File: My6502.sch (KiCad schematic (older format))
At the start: 38 parts, among them J1 ~NMI, J2 CLK Jumper, J3 Power 5V, J4 Expansion Bus, J5 Port A, J6 Port B, SW1 RESET, U1 ROM 28C256, U2 WD65C02, U3 RAM 62256, U4 74HCT00, U5 74HCT02, U6 DS1813-10, U7 74LS21, U8 WD65C22, X1 OSC

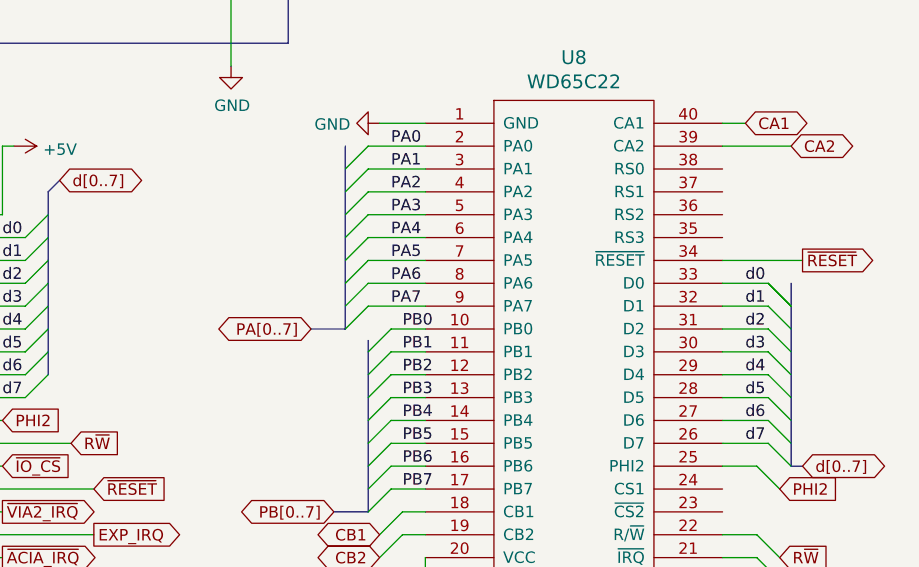
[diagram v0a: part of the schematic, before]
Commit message: Components Placed - missing wiring the VIA
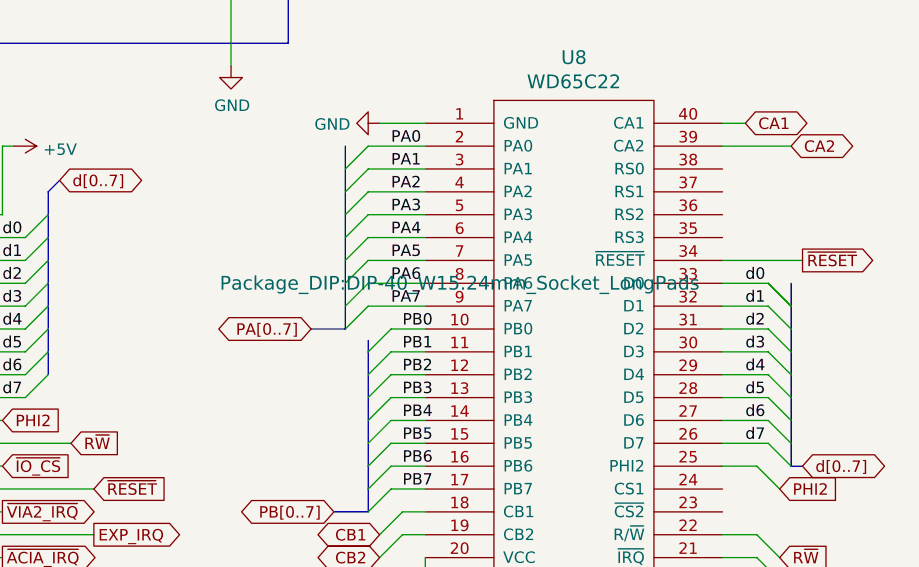
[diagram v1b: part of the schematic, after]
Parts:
- H1, H2, H3, H4: footprint (none) -> MountingHole:MountingHole_3.2mm_M3_DIN965_Pad_TopBottom
- J1: footprint (none) -> Connector_PinHeader_2.54mm:PinHeader_1x01_P2.54mm_Vertical
- TP1, TP2: footprint (none) -> TestPoint:TestPoint_THTPad_2.0x2.0mm_Drill1.0mm
- U8: footprint (none) -> Package_DIP:DIP-40_W15.24mm_Socket_LongPads
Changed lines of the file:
@@
 F 0 "TP2" V 6950 4050 50  0000 C CNN
 F 1 "~RESET" V 6850 4050 50  0000 C CNN
-F 2 "" H 7000 3800 50  0001 C CNN
+F 2 "TestPoint:TestPoint_THTPad_2.0x2.0mm_Drill1.0mm" H 7000 3800 50  0001 C CNN
 F 3 "~" H 7000 3800 50  0001 C CNN
 	1    6800 3800
@@
 F 0 "TP1" H 3602 2001 50  0000 L CNN
 F 1 "CLK" H 3602 1910 50  0000 L CNN
-F 2 "" H 3650 1900 50  0001 C CNN
+F 2 "TestPoint:TestPoint_THTPad_2.0x2.0mm_Drill1.0mm" H 3650 1900 50  0001 C CNN
 F 3 "~" H 3650 1900 50  0001 C CNN
 	1    3450 1900
@@
 F 0 "H2" V 9404 4000 50  0000 L CNN
 F 1 "MNT" V 9495 4000 50  0000 L CNN
-F 2 "" H 9450 3850 50  0001 C CNN
+F 2 "MountingHole:MountingHole_3.2mm_M3_DIN965_Pad_TopBottom" H 9450 3850 50  0001 C CNN
 F 3 "~" H 9450 3850 50  0001 C CNN
 	1    9450 3850
@@
 F 0 "H4" V 9404 4200 50  0000 L CNN
 F 1 "MNT" V 9495 4200 50  0000 L CNN
-F 2 "" H 9450 4050 50  0001 C CNN
+F 2 "MountingHole:MountingHole_3.2mm_M3_DIN965_Pad_TopBottom" H 9450 4050 50  0001 C CNN
 F 3 "~" H 9450 4050 50  0001 C CNN
 	1    9450 4050
@@
 F 0 "H1" V 9200 4100 50  0000 C CNN
 F 1 "MNT" V 9100 4100 50  0000 C CNN
-F 2 "" H 9150 3850 50  0001 C CNN
+F 2 "MountingHole:MountingHole_3.2mm_M3_DIN965_Pad_TopBottom" H 9150 3850 50  0001 C CNN
 F 3 "~" H 9150 3850 50  0001 C CNN
 	1    9150 3850
@@
 F 0 "H3" V 9200 4300 50  0000 C CNN
 F 1 "MNT" V 9100 4300 50  0000 C CNN
-F 2 "" H 9150 4050 50  0001 C CNN
+F 2 "MountingHole:MountingHole_3.2mm_M3_DIN965_Pad_TopBottom" H 9150 4050 50  0001 C CNN
 F 3 "~" H 9150 4050 50  0001 C CNN
 	1    9150 4050
@@
 F 0 "U8" H 4350 6237 60  0000 C CNN
 F 1 "WD65C22" H 4350 6131 60  0000 C CNN
-F 2 "" H 3850 5250 60  0000 C CNN
+F 2 "Package_DIP:DIP-40_W15.24mm_Socket_LongPads" H 3850 5250 60  0000 C CNN
 F 3 "" H 3850 5250 60  0000 C CNN
 	1    4350 5050
@@
 F 0 "J1" V 1056 1744 50  0000 L CNN
 F 1 "~NMI" V 1154 1744 50  0000 L CNN
-F 2 "" H 1000 1700 50  0001 C CNN
+F 2 "Connector_PinHeader_2.54mm:PinHeader_1x01_P2.54mm_Vertical" H 1000 1700 50  0001 C CNN
 F 3 "~" H 1000 1700 50  0001 C CNN
 	1    1000 1700

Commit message: PCB done minus VIA Registers - DRC Passing
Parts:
- SW1: footprint Button_Switch_THT:SW_TH_Tactile_Omron_B3F-10xx -> Button_Switch_THT:SW_PUSH_6mm_H5mm; symbol Switch:SW_Push_Dual -> Switch:SW_Push
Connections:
- net GND: no longer SW1.3
- net ~RESET: no longer SW1.4
- net OSC_OUT: now reaches J2.3 (Pin_3), X1.8 (OUT)
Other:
- moved on the sheet: J2, X1
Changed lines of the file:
@@
 L Oscillator:CXO_DIP14 X1
 U 1 1 612A3428
-P 8950 2800
-F 0 "X1" H 8550 2900 50  0000 L CNN
-F 1 "OSC" H 8700 3050 50  0000 L CNN
-F 2 "Oscillator:Oscillator_DIP-14" H 9400 2450 50  0001 C CNN
-F 3 "http://cdn-reichelt.de/documents/datenblatt/B400/OSZI.pdf" H 8850 2800 50  0001 C CNN
-	1    8950 2800
-	1    0    0    -1
-$EndComp
-Text GLabel 9500 2950 3    50   Output ~ 0
+P 8800 2900
+F 0 "X1" H 8400 3000 50  0000 L CNN
+F 1 "OSC" H 8550 3150 50  0000 L CNN
+F 2 "Oscillator:Oscillator_DIP-14" H 9250 2550 50  0001 C CNN
+F 3 "http://cdn-reichelt.de/documents/datenblatt/B400/OSZI.pdf" H 8700 2900 50  0001 C CNN
+	1    8800 2900
+	1    0    0    -1
+$EndComp
+Text GLabel 9200 3200 3    50   Output ~ 0
 CLK
 $Comp
 L power:+5V #PWR05
 U 1 1 612A648A
-P 8950 2400
-F 0 "#PWR05" H 8950 2250 50  0001 C CNN
-F 1 "+5V" H 8965 2573 50  0000 C CNN
-F 2 "" H 8950 2400 50  0001 C CNN
-F 3 "" H 8950 2400 50  0001 C CNN
-	1    8950 2400
-	1    0    0    -1
-$EndComp
-Wire Wire Line
-	8950 2400 8950 2500
+P 8800 2500
+F 0 "#PWR05" H 8800 2350 50  0001 C CNN
+F 1 "+5V" H 8815 2673 50  0000 C CNN
+F 2 "" H 8800 2500 50  0001 C CNN
+F 3 "" H 8800 2500 50  0001 C CNN
+	1    8800 2500
+	1    0    0    -1
+$EndComp
+Wire Wire Line
+	8800 2500 8800 2600
 $Comp
 L power:GND #PWR06
 U 1 1 612A9420
-P 8950 3200
-F 0 "#PWR06" H 8950 2950 50  0001 C CNN
-F 1 "GND" H 8955 3027 50  0000 C CNN
-F 2 "" H 8950 3200 50  0001 C CNN
-F 3 "" H 8950 3200 50  0001 C CNN
-	1    8950 3200
-	1    0    0    -1
-$EndComp
-NoConn ~ 8650 2800
+P 8800 3300
+F 0 "#PWR06" H 8800 3050 50  0001 C CNN
+F 1 "GND" H 8805 3127 50  0000 C CNN
+F 2 "" H 8800 3300 50  0001 C CNN
+F 3 "" H 8800 3300 50  0001 C CNN
+	1    8800 3300
+	1    0    0    -1
+$EndComp
+NoConn ~ 8500 2900
 $Comp
 L 74xx:74HCT00 U4
@@
 L Connector:Conn_01x03_Male J2
 U 1 1 61340F96
-P 9500 2500
-F 0 "J2" V 9300 2550 50  0000 R CNN
-F 1 "CLK Jumper" V 9400 2700 50  0000 R CNN
-F 2 "Connector_PinHeader_2.54mm:PinHeader_1x03_P2.54mm_Vertical" H 9500 2500 50  0001 C CNN
-F 3 "~" H 9500 2500 50  0001 C CNN
-	1    9500 2500
-	0    1    1    0
+P 9600 3000
+F 0 "J2" V 9400 3050 50  0000 R CNN
+F 1 "CLK Jumper" V 9500 3200 50  0000 R CNN
+F 2 "Connector_PinHeader_2.54mm:PinHeader_1x03_P2.54mm_Vertical" H 9600 3000 50  0001 C CNN
+F 3 "~" H 9600 3000 50  0001 C CNN
+	1    9600 3000
+	-1   0    0    1
 $EndComp
 Text GLabel 6900 3800 2    50   Output ~ 0
@@
 Power
 $Comp
-L Switch:SW_Push_Dual SW1
+L Switch:SW_Push SW1
 U 1 1 6127D438
-P 6600 4050
-F 0 "SW1" H 6646 3762 50  0000 R CNN
-F 1 "RESET" H 6700 3650 50  0000 R CNN
-F 2 "Button_Switch_THT:SW_TH_Tactile_Omron_B3F-10xx" H 6600 4250 50  0001 C CNN
-F 3 "~" H 6600 4250 50  0001 C CNN
-	1    6600 4050
-	1    0    0    -1
-$EndComp
-Wire Wire Line
-	6800 3800 6800 4050
-Wire Wire Line
-	6800 4250 6800 4350
-Wire Wire Line
-	6800 4050 6800 4250
-Connection ~ 6800 4050
-Connection ~ 6800 4250
-Wire Wire Line
-	6400 4050 6400 4250
+P 6600 4350
+F 0 "SW1" H 6700 4550 50  0000 R CNN
+F 1 "RESET" H 6700 4250 50  0000 R CNN
+F 2 "Button_Switch_THT:SW_PUSH_6mm_H5mm" H 6600 4550 50  0001 C CNN
+F 3 "~" H 6600 4550 50  0001 C CNN
+	1    6600 4350
+	1    0    0    -1
+$EndComp
+Wire Wire Line
+	6800 3800 6800 4350
+Connection ~ 6800 4350
 Wire Wire Line
 	8000 4450 8000 4600
@@
 	1    0    0    -1
 $EndComp
-Wire Wire Line
-	6400 4550 6400 4250
-Connection ~ 6400 4250
 $Comp
 L Connector:TestPoint_Probe TP2
@@
 Connection ~ 3450 1900
 Wire Wire Line
-	9400 2700 9400 2800
-Wire Wire Line
-	8950 3100 8950 3200
+	8800 3200 8800 3300
 $Comp
 L power:GND #PWR0106
 U 1 1 6363C47B
-P 9600 3200
-F 0 "#PWR0106" H 9600 2950 50  0001 C CNN
-F 1 "GND" H 9605 3027 50  0000 C CNN
-F 2 "" H 9600 3200 50  0001 C CNN
-F 3 "" H 9600 3200 50  0001 C CNN
-	1    9600 3200
-	1    0    0    -1
-$EndComp
-Wire Wire Line
-	9500 2700 9500 2950
-Text Notes 8550 2150 0    50   ~ 0
+P 9350 3250
+F 0 "#PWR0106" H 9350 3000 50  0001 C CNN
+F 1 "GND" H 9355 3077 50  0000 C CNN
+F 2 "" H 9350 3250 50  0001 C CNN
+F 3 "" H 9350 3250 50  0001 C CNN
+	1    9350 3250
+	1    0    0    -1
+$EndComp
+Text Notes 8400 2250 0    50   ~ 0
 Clock
 Text GLabel 3000 1400 1    50   Output ~ 0
@@
 F 0 "U8" H 4350 6237 60  0000 C CNN
 F 1 "WD65C22" H 4350 6131 60  0000 C CNN
-F 2 "Package_DIP:DIP-40_W15.24mm_Socket_LongPads" H 3850 5250 60  0000 C CNN
+F 2 "Package_DIP:DIP-40_W15.24mm_Socket_LongPads" H 3850 5250 60  0001 C CNN
 F 3 "" H 3850 5250 60  0000 C CNN
 	1    4350 5050
 	1    0    0    -1
 $EndComp
-Text Label 9150 2900 0    50   ~ 0
-CLK_OUT
-Wire Wire Line
-	9600 2700 9600 3200
 Wire Wire Line
 	10150 3400 10150 2950
@@
 Wire Wire Line
 	11000 2500 11000 2950
-Wire Wire Line
-	9250 2800 9400 2800
 Text Notes 6150 650  0    50   ~ 0
 ROM 32K (24K in Use)
@@
 Wire Wire Line
 	10950 4350 10950 4500
+Wire Wire Line
+	6400 4350 6400 4550
+Text Label 9100 2900 0    50   ~ 0
+OSC_OUT
+Wire Wire Line
+	9100 2900 9400 2900
+Wire Wire Line
+	9400 3000 9200 3000
+Wire Wire Line
+	9200 3000 9200 3200
+Wire Wire Line
+	9400 3100 9350 3100
+Wire Wire Line
+	9350 3100 9350 3250
 Wire Bus Line
 	5550 6900 5550 7300

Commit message: V1.5 Ready - Full board CPU,RAM,ROM,VIA
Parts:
- D1: value LED -> POWER
- JP2: renamed from J2; value CLK Jumper -> CLK SEL
- renumbered C2 to C1, C6 to C2, C7 to C6, C8 to C7, C1 to C8, U2 to U1, U1 to U2, U7 to U6, U8 to U7, U6 to U8
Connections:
- net a0: now also U7.38 (RS0)
- net a1: now also U7.37 (RS1)
- net a12: now also U7.24 (CS1)
- net a2: now also U7.36 (RS2)
- net a3: now also U7.35 (RS3)
- net ~IO_CS: now also U7.23 (~CS2)
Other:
- note added: "VIA 1\n$9000 - $900F"
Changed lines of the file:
@@
 $EndComp
 $Comp
-L DS1813-10:DS1813-10 U6
+L DS1813-10:DS1813-10 U8
 U 1 1 61278A1B
 P 7200 4350
-F 0 "U6" H 7400 4700 50  0000 C CNN
+F 0 "U8" H 7400 4700 50  0000 C CNN
 F 1 "DS1813-10" H 7400 4600 50  0000 C CNN
 F 2 "Package_TO_SOT_THT:TO-92" H 7200 4350 50  0001 L BNN
@@
 	7600 6250 7700 6250
 $Comp
-L Connector:Conn_01x03_Male J2
+L Connector:Conn_01x03_Male JP2
 U 1 1 61340F96
 P 9600 3000
-F 0 "J2" V 9400 3050 50  0000 R CNN
-F 1 "CLK Jumper" V 9500 3200 50  0000 R CNN
+F 0 "JP2" V 9400 3050 50  0000 R CNN
+F 1 "CLK SEL" V 9500 3200 50  0000 R CNN
 F 2 "Connector_PinHeader_2.54mm:PinHeader_1x03_P2.54mm_Vertical" H 9600 3000 50  0001 C CNN
 F 3 "~" H 9600 3000 50  0001 C CNN
@@
 $EndComp
 $Comp
-L Memory_EEPROM:28C256 U1
+L Memory_EEPROM:28C256 U2
 U 1 1 61405640
 P 7250 2000
-F 0 "U1" H 7250 3281 50  0000 C CNN
+F 0 "U2" H 7250 3281 50  0000 C CNN
 F 1 "ROM 28C256" H 7250 3190 50  0000 C CNN
 F 2 "Package_DIP:DIP-28_W15.24mm_Socket_LongPads" H 7250 2000 50  0001 C CNN
@@
 	5450 2150 5300 2150
 $Comp
-L Device:C C7
+L Device:C C6
 U 1 1 6163A5A8
 P 10450 2950
-F 0 "C7" H 10565 2996 50  0000 L CNN
+F 0 "C6" H 10565 2996 50  0000 L CNN
 F 1 "0.1uF" H 10565 2905 50  0000 L CNN
 F 2 "Capacitor_THT:C_Disc_D4.3mm_W1.9mm_P5.00mm" H 10488 2800 50  0001 C CNN
@@
 $EndComp
 $Comp
-L Device:C C2
+L Device:C C1
 U 1 1 6163E271
 P 10450 5200
-F 0 "C2" H 10565 5246 50  0000 L CNN
+F 0 "C1" H 10565 5246 50  0000 L CNN
 F 1 "0.1uF" H 10565 5155 50  0000 L CNN
 F 2 "Capacitor_THT:C_Disc_D4.3mm_W1.9mm_P5.00mm" H 10488 5050 50  0001 C CNN
@@
 Connection ~ 10150 5200
 $Comp
-L Device:CP C1
+L Device:CP C8
 U 1 1 6163F681
 P 10450 5650
-F 0 "C1" H 10568 5696 50  0000 L CNN
+F 0 "C8" H 10568 5696 50  0000 L CNN
 F 1 "100uF" H 10568 5605 50  0000 L CNN
 F 2 "Capacitor_THT:CP_Radial_D8.0mm_P3.80mm" H 10488 5500 50  0001 C CNN
@@
 	6900 3800 6800 3800
 $Comp
-L 74xx:74LS21 U7
+L 74xx:74LS21 U6
 U 1 1 61B46D36
 P 9150 1550
-F 0 "U7" H 9150 1925 50  0000 C CNN
+F 0 "U6" H 9150 1925 50  0000 C CNN
 F 1 "74LS21" H 9150 1834 50  0000 C CNN
 F 2 "Package_DIP:DIP-14_W7.62mm_Socket_LongPads" H 9150 1550 50  0001 C CNN
@@
 $EndComp
 $Comp
-L 74xx:74LS21 U7
+L 74xx:74LS21 U6
 U 2 1 61B48F07
 P 9900 6800
-F 0 "U7" H 9900 7175 50  0000 C CNN
+F 0 "U6" H 9900 7175 50  0000 C CNN
 F 1 "74LS21" H 9900 7084 50  0000 C CNN
 F 2 "Package_DIP:DIP-14_W7.62mm_Socket_LongPads" H 9900 6800 50  0001 C CNN
@@
 	1750 6150 2250 6150
 $Comp
-L Device:C C6
+L Device:C C2
 U 1 1 63306EB2
 P 10450 3400
-F 0 "C6" H 10565 3446 50  0000 L CNN
+F 0 "C2" H 10565 3446 50  0000 L CNN
 F 1 "0.1uF" H 10565 3355 50  0000 L CNN
 F 2 "Capacitor_THT:C_Disc_D4.3mm_W1.9mm_P5.00mm" H 10488 3250 50  0001 C CNN
@@
 $EndComp
 $Comp
-L 74xx:74LS21 U7
+L 74xx:74LS21 U6
 U 3 1 61B4DE7C
 P 10500 850
-F 0 "U7" H 10450 850 50  0000 L CNN
+F 0 "U6" H 10450 850 50  0000 L CNN
 F 1 "74LS21" V 10730 805 50  0000 L CNN
 F 2 "Package_DIP:DIP-14_W7.62mm_Socket_LongPads" H 10500 850 50  0001 C CNN
@@
 $EndComp
 $Comp
-L 65xx:WD65C02 U2
+L 65xx:WD65C02 U1
 U 1 1 612219A0
 P 2200 2500
-F 0 "U2" H 2200 3687 60  0000 C CNN
+F 0 "U1" H 2200 3687 60  0000 C CNN
 F 1 "WD65C02" H 2200 3581 60  0000 C CNN
 F 2 "Package_DIP:DIP-40_W15.24mm_Socket_LongPads" H 1700 2700 60  0001 C CNN
@@
 Expansion Bus
 $Comp
-L 65xx:WD65C22 U8
+L 65xx:WD65C22 U7
 U 1 1 651371E7
 P 4350 5050
-F 0 "U8" H 4350 6237 60  0000 C CNN
+F 0 "U7" H 4350 6237 60  0000 C CNN
 F 1 "WD65C22" H 4350 6131 60  0000 C CNN
 F 2 "Package_DIP:DIP-40_W15.24mm_Socket_LongPads" H 3850 5250 60  0001 C CNN
@@
 Text GLabel 3300 5850 0    50   BiDi ~ 0
 PB[0..7]
-Text GLabel 5100 4150 2    50   BiDi ~ 0
+Text GLabel 5000 3900 1    50   BiDi ~ 0
 CA1
-Text GLabel 5300 4250 2    50   BiDi ~ 0
+Text GLabel 5100 3900 1    50   BiDi ~ 0
 CA2
 Text GLabel 3500 5950 0    50   BiDi ~ 0
@@
 Wire Wire Line
 	3600 5950 3700 5950
-Wire Wire Line
-	5000 4150 5100 4150
-Wire Wire Line
-	5000 4250 5300 4250
 Wire Wire Line
 	3500 6250 3700 6250
@@
 	3050 7650 2950 7650
 $Comp
-L Device:C C8
+L Device:C C7
 U 1 1 66A97774
 P 10450 2500
-F 0 "C8" H 10565 2546 50  0000 L CNN
+F 0 "C7" H 10565 2546 50  0000 L CNN
 F 1 "0.1uF" H 10565 2455 50  0000 L CNN
 F 2 "Capacitor_THT:C_Disc_D4.3mm_W1.9mm_P5.00mm" H 10488 2350 50  0001 C CNN
@@
 P 10950 4200
 F 0 "D1" V 10989 4082 50  0000 R CNN
-F 1 "LED" V 10898 4082 50  0000 R CNN
+F 1 "POWER" V 10898 4082 50  0000 R CNN
 F 2 "LED_THT:LED_D3.0mm" H 10950 4200 50  0001 C CNN
 F 3 "~" H 10950 4200 50  0001 C CNN
@@
 Wire Wire Line
 	9350 3100 9350 3250
+Entry Wire Line
+	5200 4350 5300 4250
+Entry Wire Line
+	5200 4450 5300 4350
+Entry Wire Line
+	5200 4550 5300 4450
+Entry Wire Line
+	5200 4650 5300 4550
+Text GLabel 5350 3700 2    50   BiDi ~ 0
+a[0..15]
+Wire Wire Line
+	5000 4350 5200 4350
+Wire Wire Line
+	5200 4450 5000 4450
+Wire Wire Line
+	5000 4550 5200 4550
+Wire Wire Line
+	5200 4650 5000 4650
+Text Label 5100 4350 0    50   ~ 0
+a0
+Text Label 5100 4450 0    50   ~ 0
+a1
+Text Label 5100 4550 0    50   ~ 0
+a2
+Text Label 5100 4650 0    50   ~ 0
+a3
+Wire Bus Line
+	5300 3750 5350 3700
+Wire Wire Line
+	5000 4150 5000 3900
+Wire Wire Line
+	5000 4250 5100 4250
+Wire Wire Line
+	5100 4250 5100 3900
+Entry Wire Line
+	5300 4100 5400 4200
+Wire Wire Line
+	5000 5750 5150 5750
+Wire Wire Line
+	5150 5750 5250 5850
+Wire Wire Line
+	5250 5850 5750 5850
+Wire Wire Line
+	5750 5850 5750 4200
+Wire Wire Line
+	5750 4200 5400 4200
+Text Label 5400 4200 0    50   ~ 0
+a12
+Text GLabel 5450 5950 2    50   Input ~ 0
+~IO_CS
+Wire Wire Line
+	5000 5850 5150 5850
+Wire Wire Line
+	5150 5850 5250 5950
+Wire Wire Line
+	5250 5950 5450 5950
 Wire Bus Line
 	5550 6900 5550 7300
@@
 	3100 3200 3100 3800
 Wire Bus Line
+	5300 3750 5300 4550
+Wire Bus Line
 	3450 5100 3450 5850
 Wire Bus Line
@@
 Wire Bus Line
 	950  4750 950  6350
+Text Notes 3450 3800 0    50   ~ 0
+VIA 1\n$9000 - $900F
 $EndSCHEMATC

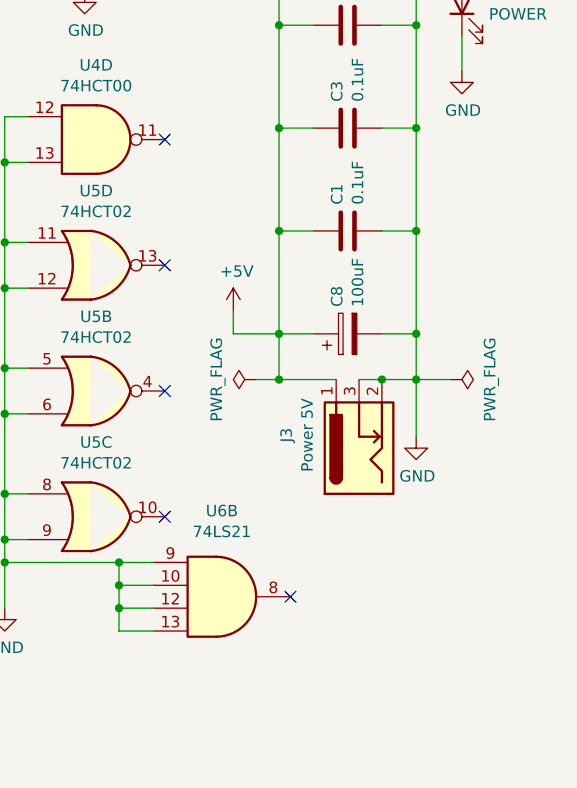
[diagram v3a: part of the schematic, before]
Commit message: Gerber file deleted had errors. New Schematic with power leads and GND Test
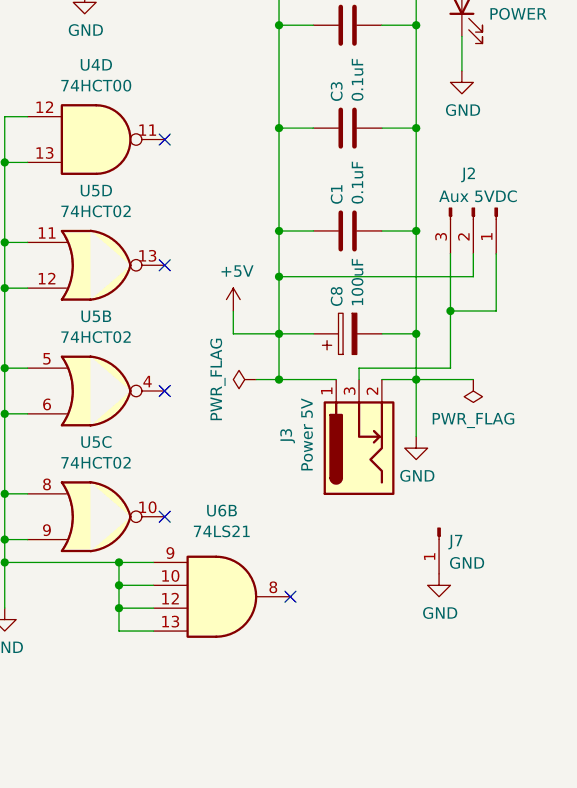
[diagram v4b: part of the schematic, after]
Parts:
- added J2: Aux 5VDC, symbol Connector:Conn_01x03_Male
- added J7: GND, Connector_PinHeader_2.54mm:PinHeader_1x01_P2.54mm_Vertical, symbol Connector:Conn_01x01_Male
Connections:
- net +5V: now also J2.2 (Pin_2)
- net GND: now also J7.1 (Pin_1); no longer J3.3
- new net: J2.1 (Pin_1), J2.3 (Pin_3), J3.3
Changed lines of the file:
@@
 Wire Wire Line
 	4900 3000 4900 2850
-$Comp
-L power:PWR_FLAG #FLG0102
-U 1 1 6194FE47
-P 10900 5850
-F 0 "#FLG0102" H 10900 5925 50  0001 C CNN
-F 1 "PWR_FLAG" H 10900 6023 50  0000 C CNN
-F 2 "" H 10900 5850 50  0001 C CNN
-F 3 "~" H 10900 5850 50  0001 C CNN
-	1    10900 5850
-	0    1    1    0
-$EndComp
 Wire Wire Line
 	6900 3800 6800 3800
@@
 	10750 5200 10750 5650
 Wire Wire Line
-	10150 5200 10150 5650
+	10150 5200 10150 5400
 Wire Wire Line
 	10300 5650 10150 5650
@@
 Connection ~ 10750 5850
 Wire Wire Line
-	10750 5850 10900 5850
+	10750 5850 11000 5850
 Text Notes 9800 650  0    50   ~ 0
 Power
@@
 Wire Wire Line
 	9300 3850 9350 3850
-Wire Wire Line
-	10500 5850 10600 5850
-Connection ~ 10600 5850
 $Comp
 L Device:C C3
@@
 Wire Wire Line
 	5250 5950 5450 5950
-Wire Bus Line
-	5550 6900 5550 7300
-Wire Bus Line
-	4350 7000 4350 7450
-Wire Bus Line
-	3300 6900 3300 7300
-Wire Bus Line
-	2100 7000 2100 7450
-Wire Bus Line
-	6650 5500 6650 6700
-Wire Bus Line
-	3100 3200 3100 3800
-Wire Bus Line
-	5300 3750 5300 4550
-Wire Bus Line
-	3450 5100 3450 5850
-Wire Bus Line
-	3350 4250 3350 5050
-Wire Bus Line
-	5300 4850 5300 5650
-Wire Bus Line
-	2050 4450 2050 5250
-Wire Bus Line
-	5550 1250 5550 2050
-Wire Bus Line
-	7950 1100 7950 1900
-Wire Bus Line
-	3200 2400 3200 3150
-Wire Bus Line
-	1100 2400 1100 3800
-Wire Bus Line
-	4200 1350 4200 2850
-Wire Bus Line
-	6550 1100 6550 2600
-Wire Bus Line
-	950  4750 950  6350
 Text Notes 3450 3800 0    50   ~ 0
 VIA 1\n$9000 - $900F
+$Comp
+L Connector:Conn_01x03_Male J2
+U 1 1 6344051E
+P 11000 5100
+F 0 "J2" V 10850 5050 50  0000 L CNN
+F 1 "Aux 5VDC" V 10950 4950 50  0000 L CNN
+F 2 "" H 11000 5100 50  0001 C CNN
+F 3 "~" H 11000 5100 50  0001 C CNN
+	1    11000 5100
+	0    1    1    0
+$EndComp
+Wire Wire Line
+	10500 5850 10500 5800
+Wire Wire Line
+	10500 5800 10900 5800
+$Comp
+L power:PWR_FLAG #FLG0102
+U 1 1 6194FE47
+P 11000 5850
+F 0 "#FLG0102" H 11000 5925 50  0001 C CNN
+F 1 "PWR_FLAG" H 11000 6023 50  0000 C CNN
+F 2 "" H 11000 5850 50  0001 C CNN
+F 3 "~" H 11000 5850 50  0001 C CNN
+	1    11000 5850
+	-1   0    0    1
+$EndComp
+Wire Wire Line
+	10900 5300 10900 5550
+Wire Wire Line
+	10900 5550 11100 5550
+Wire Wire Line
+	11100 5550 11100 5300
+Wire Wire Line
+	10900 5550 10900 5800
+Connection ~ 10900 5550
+Wire Wire Line
+	10150 5400 11000 5400
+Wire Wire Line
+	11000 5400 11000 5300
+Connection ~ 10150 5400
+Wire Wire Line
+	10150 5400 10150 5650
+Wire Bus Line
+	5550 6900 5550 7300
+Wire Bus Line
+	4350 7000 4350 7450
+Wire Bus Line
+	3300 6900 3300 7300
+Wire Bus Line
+	2100 7000 2100 7450
+Wire Bus Line
+	6650 5500 6650 6700
+Wire Bus Line
+	3100 3200 3100 3800
+Wire Bus Line
+	5300 3750 5300 4550
+Wire Bus Line
+	3450 5100 3450 5850
+Wire Bus Line
+	3350 4250 3350 5050
+Wire Bus Line
+	5300 4850 5300 5650
+Wire Bus Line
+	2050 4450 2050 5250
+Wire Bus Line
+	5550 1250 5550 2050
+Wire Bus Line
+	7950 1100 7950 1900
+Wire Bus Line
+	3200 2400 3200 3150
+Wire Bus Line
+	1100 2400 1100 3800
+Wire Bus Line
+	4200 1350 4200 2850
+Wire Bus Line
+	6550 1100 6550 2600
+Wire Bus Line
+	950  4750 950  6350
+$Comp
+L Connector:Conn_01x01_Male J7
+U 1 1 6375840F
+P 10850 6500
+F 0 "J7" V 10906 6544 50  0000 L CNN
+F 1 "GND" V 11004 6544 50  0000 L CNN
+F 2 "Connector_PinHeader_2.54mm:PinHeader_1x01_P2.54mm_Vertical" H 10850 6500 50  0001 C CNN
+F 3 "~" H 10850 6500 50  0001 C CNN
+	1    10850 6500
+	0    1    1    0
+$EndComp
+$Comp
+L power:GND #PWR015
+U 1 1 63759C59
+P 10850 6700
+F 0 "#PWR015" H 10850 6450 50  0001 C CNN
+F 1 "GND" H 10855 6527 50  0000 C CNN
+F 2 "" H 10850 6700 50  0001 C CNN
+F 3 "" H 10850 6700 50  0001 C CNN
+	1    10850 6700
+	1    0    0    -1
+$EndComp
 $EndSCHEMATC
